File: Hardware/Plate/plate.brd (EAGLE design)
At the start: 68.6 x 68.6 mm, 5 parts

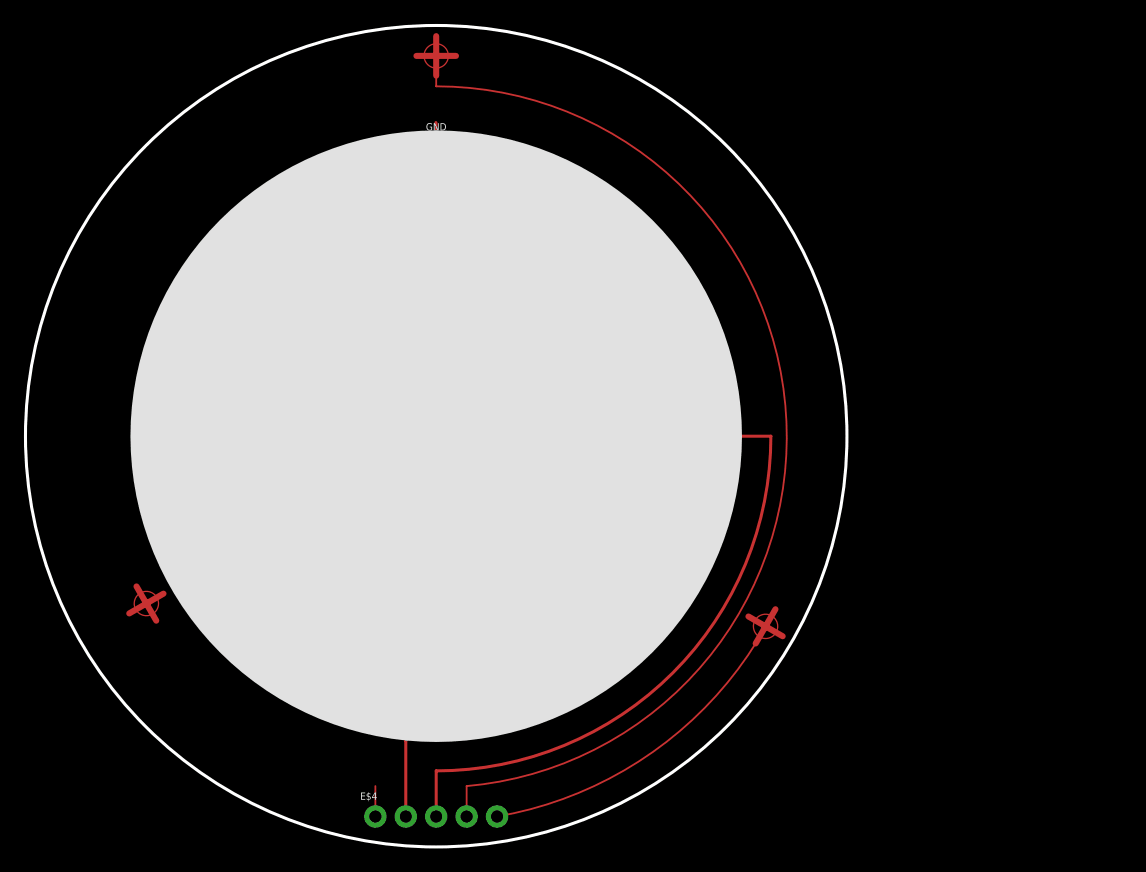
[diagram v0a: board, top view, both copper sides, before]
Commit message: Fixed pour isolation
Also added labels and made orientation more clear for assembly
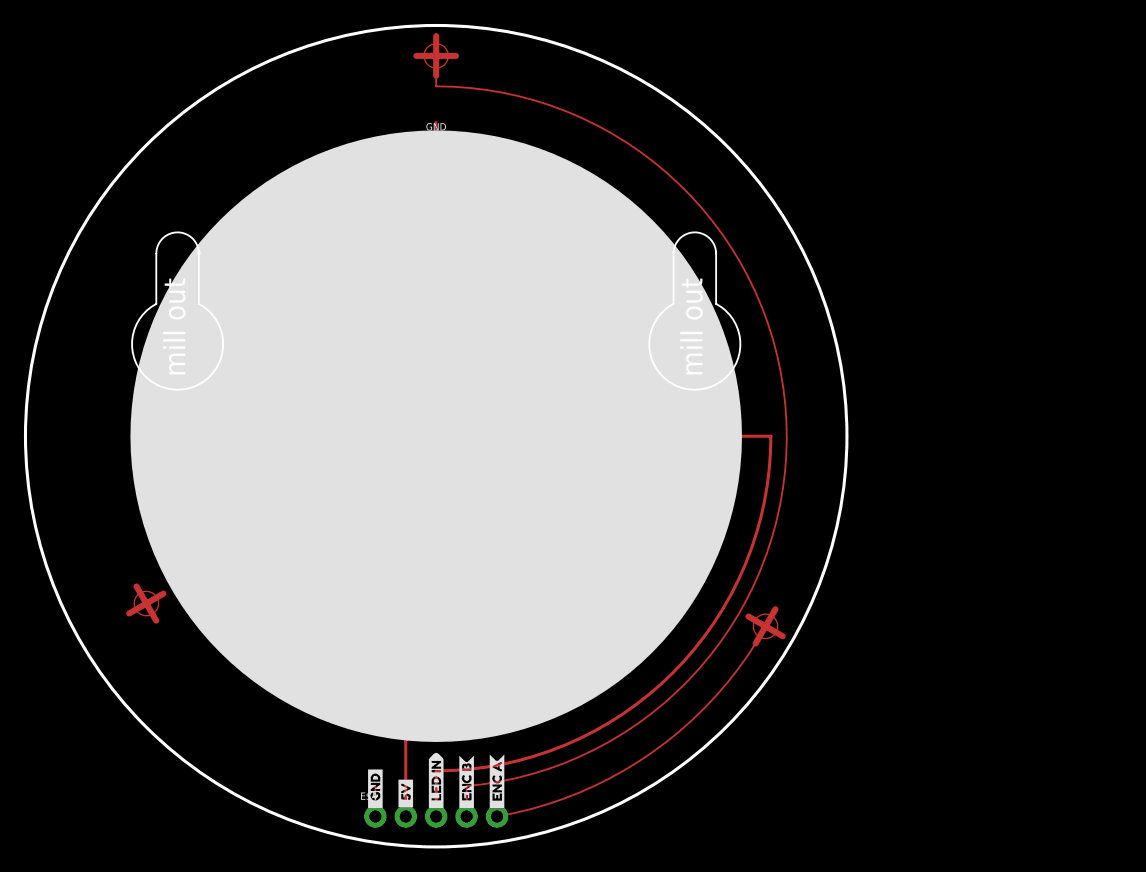
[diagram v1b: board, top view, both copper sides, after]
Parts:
- removed E$8: (no value), SparkFun-Hardware:STANDOFF-ELECTRICAL
- added E$1: (no value), SparkFun-Hardware:STAND-OFF-TIGHT
- added E$2: (no value), buzzard_labels (41):_ENC_A0
- added E$3: (no value), buzzard_labels (41):_ENC_B1
- added E$5: (no value), buzzard_labels (41):_LED_IN2
- added E$6: (no value), buzzard_labels (44):_GND0
- added E$7: (no value), buzzard_labels (42):_5V0
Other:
- outline, holes or cut-outs redrawn
- board text added: "mill out"
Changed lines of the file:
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@@
 <?xml version="1.0" encoding="utf-8"?>
 <!DOCTYPE eagle SYSTEM "eagle.dtd">
-<eagle version="7.7.0">
+<eagle version="9.0.1">
 <drawing>
 <settings>
 <setting alwaysvectorfont="yes"/>
+<setting keepoldvectorfont="yes"/>
 <setting verticaltext="up"/>
 </settings>
@@
 <layer number="19" name="Unrouted" color="6" fill="1" visible="yes" active="yes"/>
 <layer number="20" name="Dimension" color="15" fill="1" visible="yes" active="yes"/>
-<layer number="21" name="tPlace" color="16" fill="1" visible="no" active="yes"/>
+<layer number="21" name="tPlace" color="16" fill="1" visible="yes" active="yes"/>
 <layer number="22" name="bPlace" color="14" fill="1" visible="yes" active="yes"/>
 <layer number="23" name="tOrigins" color="15" fill="1" visible="yes" active="yes"/>
 <layer number="24" name="bOrigins" color="15" fill="1" visible="yes" active="yes"/>
-<layer number="25" name="tNames" color="7" fill="1" visible="yes" active="yes"/>
-<layer number="26" name="bNames" color="7" fill="1" visible="yes" active="yes"/>
-<layer number="27" name="tValues" color="7" fill="1" visible="yes" active="yes"/>
-<layer number="28" name="bValues" color="7" fill="1" visible="yes" active="yes"/>
+<layer number="25" name="tNames" color="7" fill="1" visible="no" active="yes"/>
+<layer number="26" name="bNames" color="7" fill="1" visible="no" active="yes"/>
+<layer number="27" name="tValues" color="7" fill="1" visible="no" active="yes"/>
+<layer number="28" name="bValues" color="7" fill="1" visible="no" active="yes"/>
 <layer number="29" name="tStop" color="7" fill="3" visible="yes" active="yes"/>
 <layer number="30" name="bStop" color="7" fill="6" visible="yes" active="yes"/>
-<layer number="31" name="tCream" color="7" fill="4" visible="yes" active="yes"/>
-<layer number="32" name="bCream" color="7" fill="5" visible="yes" active="yes"/>
-<layer number="33" name="tFinish" color="6" fill="3" visible="yes" active="yes"/>
-<layer number="34" name="bFinish" color="6" fill="6" visible="yes" active="yes"/>
-<layer number="35" name="tGlue" color="7" fill="4" visible="yes" active="yes"/>
-<layer number="36" name="bGlue" color="7" fill="5" visible="yes" active="yes"/>
-<layer number="37" name="tTest" color="7" fill="1" visible="yes" active="yes"/>
-<layer number="38" name="bTest" color="7" fill="1" visible="yes" active="yes"/>
+<layer number="31" name="tCream" color="7" fill="4" visible="no" active="yes"/>
+<layer number="32" name="bCream" color="7" fill="5" visible="no" active="yes"/>
+<layer number="33" name="tFinish" color="6" fill="3" visible="no" active="yes"/>
+<layer number="34" name="bFinish" color="6" fill="6" visible="no" active="yes"/>
+<layer number="35" name="tGlue" color="7" fill="4" visible="no" active="yes"/>
+<layer number="36" name="bGlue" color="7" fill="5" visible="no" active="yes"/>
+<layer number="37" name="tTest" color="7" fill="1" visible="no" active="yes"/>
+<layer number="38" name="bTest" color="7" fill="1" visible="no" active="yes"/>
 <layer number="39" name="tKeepout" color="4" fill="11" visible="yes" active="yes"/>
 <layer number="40" name="bKeepout" color="1" fill="11" visible="yes" active="yes"/>
 <layer number="41" name="tRestrict" color="4" fill="10" visible="yes" active="yes"/>
 <layer number="42" name="bRestrict" color="1" fill="10" visible="yes" active="yes"/>
-<layer number="43" name="vRestrict" color="2" fill="10" visible="yes" active="yes"/>
-<layer number="44" name="Drills" color="7" fill="1" visible="yes" active="yes"/>
+<layer number="43" name="vRestrict" color="2" fill="10" visible="no" active="yes"/>
+<layer number="44" name="Drills" color="7" fill="1" visible="no" active="yes"/>
 <layer number="45" name="Holes" color="7" fill="1" visible="yes" active="yes"/>
-<layer number="46" name="Milling" color="3" fill="1" visible="yes" active="yes"/>
-<layer number="47" name="Measures" color="7" fill="1" visible="yes" active="yes"/>
-<layer number="48" name="Document" color="7" fill="1" visible="yes" active="yes"/>
-<layer number="49" name="Reference" color="7" fill="1" visible="yes" active="yes"/>
-<layer number="50" name="dxf" color="7" fill="1" visible="yes" active="yes"/>
+<layer number="46" name="Milling" color="3" fill="1" visible="no" active="yes"/>
+<layer number="47" name="Measures" color="7" fill="1" visible="no" active="yes"/>
+<layer number="48" name="Document" color="7" fill="1" visible="no" active="yes"/>
+<layer number="49" name="Reference" color="7" fill="1" visible="no" active="yes"/>
+<layer number="50" name="dxf" color="7" fill="1" visible="no" active="yes"/>
 <layer number="51" name="tDocu" color="6" fill="1" visible="yes" active="yes"/>
-<layer number="52" name="bDocu" color="7" fill="1" visible="yes" active="yes"/>
+<layer number="52" name="bDocu" color="7" fill="1" visible="no" active="yes"/>
 <layer number="91" name="Nets" color="2" fill="1" visible="no" active="no"/>
 <layer number="92" name="Busses" color="1" fill="1" visible="no" active="no"/>
@@
 <layer number="59" name="tCarbon" color="7" fill="1" visible="no" active="no"/>
 <layer number="60" name="bCarbon" color="7" fill="1" visible="no" active="no"/>
-<layer number="88" name="SimResults" color="9" fill="1" visible="yes" active="yes"/>
-<layer number="89" name="SimProbes" color="9" fill="1" visible="yes" active="yes"/>
+<layer number="88" name="SimResults" color="9" fill="1" visible="no" active="no"/>
+<layer number="89" name="SimProbes" color="9" fill="1" visible="no" active="no"/>
 <layer number="90" name="Modules" color="5" fill="1" visible="no" active="no"/>
 <layer number="97" name="Info" color="7" fill="1" visible="no" active="no"/>
@@
 <vertex x="-23.74135" y="-12.235146875"/>
 </polygon>
+<polygon width="0.254" layer="41">
+<vertex x="-1.683934375" y="32.24530625" curve="-90"/>
+<vertex x="-0.49013125" y="33.71850625"/>
+<vertex x="-1.683940625" y="33.718503125"/>
+</polygon>
+<polygon width="0.254" layer="41">
+<vertex x="-0.49530625" y="30.091465625" curve="-90"/>
+<vertex x="-1.66370625" y="31.25986875"/>
+<vertex x="-1.663703125" y="30.091459375"/>
+</polygon>
+<polygon width="0.254" layer="41">
+<vertex x="29.071409375" y="-17.26050625" curve="-90"/>
+<vertex x="26.9412125" y="-17.812921875"/>
+<vertex x="28.20631875" y="-18.551009375"/>
+</polygon>
+<wire x1="-23.368" y1="15.24" x2="-23.368" y2="11.049" width="0.1524" layer="20"/>
+<wire x1="-19.812" y1="15.367" x2="-19.812" y2="15.24" width="0.254" layer="20"/>
+<wire x1="-19.812" y1="15.24" x2="-19.812" y2="11.049" width="0.1524" layer="20"/>
+<wire x1="-23.368" y1="11.049" x2="-19.812" y2="11.049" width="0.1524" layer="20" curve="304.304843"/>
+<wire x1="-19.812" y1="15.24" x2="-23.368" y2="15.24" width="0.1524" layer="20" curve="180"/>
+<text x="-20.955" y="4.953" size="1.778" layer="20" font="vector" ratio="15" rot="R90">mill out</text>
+<wire x1="19.812" y1="15.24" x2="19.812" y2="11.049" width="0.1524" layer="20"/>
+<wire x1="23.368" y1="15.367" x2="23.368" y2="15.24" width="0.1524" layer="20"/>
+<wire x1="23.368" y1="15.24" x2="23.368" y2="11.049" width="0.1524" layer="20"/>
+<wire x1="19.812" y1="11.049" x2="23.368" y2="11.049" width="0.1524" layer="20" curve="304.304843"/>
+<wire x1="23.368" y1="15.24" x2="19.812" y2="15.24" width="0.1524" layer="20" curve="180"/>
+<text x="22.225" y="4.953" size="1.778" layer="20" font="vector" ratio="15" rot="R90">mill out</text>
 </plain>
 <attributes>
@@
 <param name="dpMaxLengthDifference" value="10mm"/>
 <param name="dpGapFactor" value="2.5"/>
-<param name="checkGrid" value="0"/>
 <param name="checkAngle" value="1"/>
 <param name="checkFont" value="1"/>
 <param name="checkRestrict" value="1"/>
+<param name="checkStop" value="0"/>
+<param name="checkValues" value="0"/>
 <param name="useDiameter" value="13"/>
 <param name="maxErrors" value="50"/>
@@
 <elements>
 <element name="E$4" library="SparkFun-Connectors" package="1X05_NO_SILK" value="" x="-5.08" y="-31.75"/>
-<element name="E$8" library="SparkFun-Hardware" package="STANDOFF-ELECTRICAL" value="" x="-22.225" y="0"/>
 <element name="E$9" library="SparkFun-Hardware" package="STANDOFF-ELECTRICAL" value="" x="0" y="-22.225"/>
 <element name="E$10" library="SparkFun-Hardware" package="STANDOFF-ELECTRICAL" value="" x="22.225" y="0"/>
 <element name="GND" library="SparkFun-Hardware" package="STANDOFF-ELECTRICAL" value="" x="0" y="22.225"/>
+<element name="E$1" library="SparkFun-Hardware" package="STAND-OFF-TIGHT" value="" x="-22.225" y="0"/>
+<element name="E$2" library="buzzard_labels (41)" package="_ENC_A0" value="" x="5.08" y="-31.4452" rot="R90"/>
+<element name="E$3" library="buzzard_labels (41)" package="_ENC_B1" value="" x="2.54" y="-31.3944" rot="R90"/>
+<element name="E$5" library="buzzard_labels (41)" package="_LED_IN2" value="" x="0" y="-31.3944" rot="R90"/>
+<element name="E$7" library="buzzard_labels (42)" package="_5V0" value="" x="-2.54" y="-31.3436" rot="R90"/>
+<element name="E$6" library="buzzard_labels (44)" package="_GND0" value="" x="-5.08" y="-31.3944" rot="R90"/>
 </elements>
 <signals>

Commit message: Cleanup
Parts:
- added E$11: (no value), SparkX:SPARKX-LARGE
- added E$12: (no value), SparkFun-Aesthetics:OSHW-LOGO-M
- added E$13: (no value), buzzard_labels (44):_GND0
- added E$14: (no value), buzzard_labels (42):_5V0
- added E$15: (no value), buzzard_labels (41):_LED_IN2
- added E$16: (no value), buzzard_labels (41):_ENC_B1
- added E$17: (no value), buzzard_labels (41):_ENC_A0
- added E$8: (no value), buzzard_labels (47):ROTARY_DIAL0
- moved E$1 22.9 mm to (0.64, 0.00)
- moved E$10 22.9 mm to (45.1, 0.00)
- moved E$2 22.9 mm to (27.9, -31.4)
- moved E$3 22.9 mm to (25.4, -31.4)
- moved E$4 22.9 mm to (17.8, -31.8)
- moved E$5 22.9 mm to (22.9, -31.4)
- moved E$6 22.9 mm to (17.8, -31.4)
- moved E$7 22.9 mm to (20.3, -31.3)
- moved E$9 22.9 mm to (22.9, -22.2)
- moved GND 22.9 mm to (22.9, 22.2)
